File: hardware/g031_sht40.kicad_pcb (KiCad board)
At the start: 2 copper layers, 75 x 47 mm, 29 parts, among them J1 Screw_Terminal_01x02, J2 Conn_01x06_Pin, J3 Conn_01x02_Pin, J4 Screw_Terminal_01x02, J5 Conn_01x03_Pin, J6 Conn_01x04_Pin, J7 Conn_01x04_Pin, J8 Conn_01x08_Pin, SW1 SW_Push, U1 AEM10941 module, U2 SHT40 module, U3 STM32G031F6Px, U4 E-Ink display module

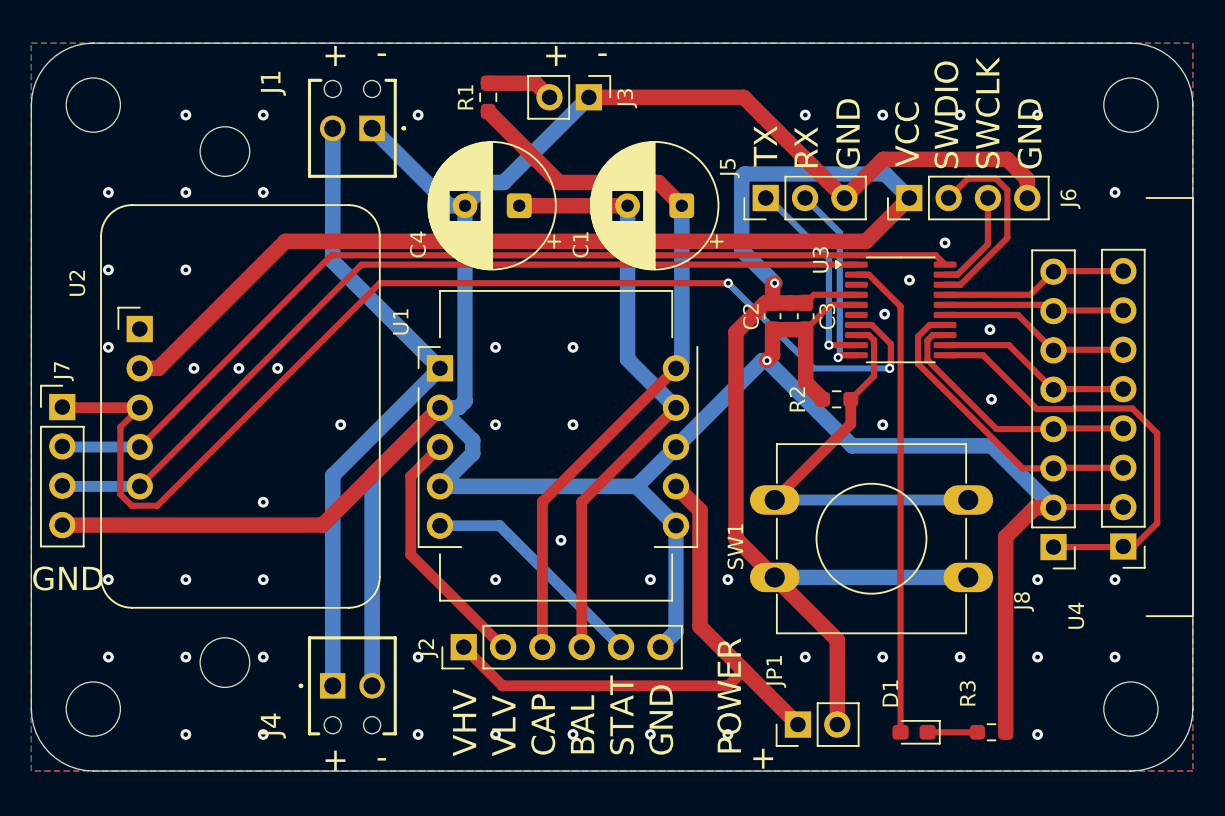
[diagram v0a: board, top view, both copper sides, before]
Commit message: Add Status pin connection
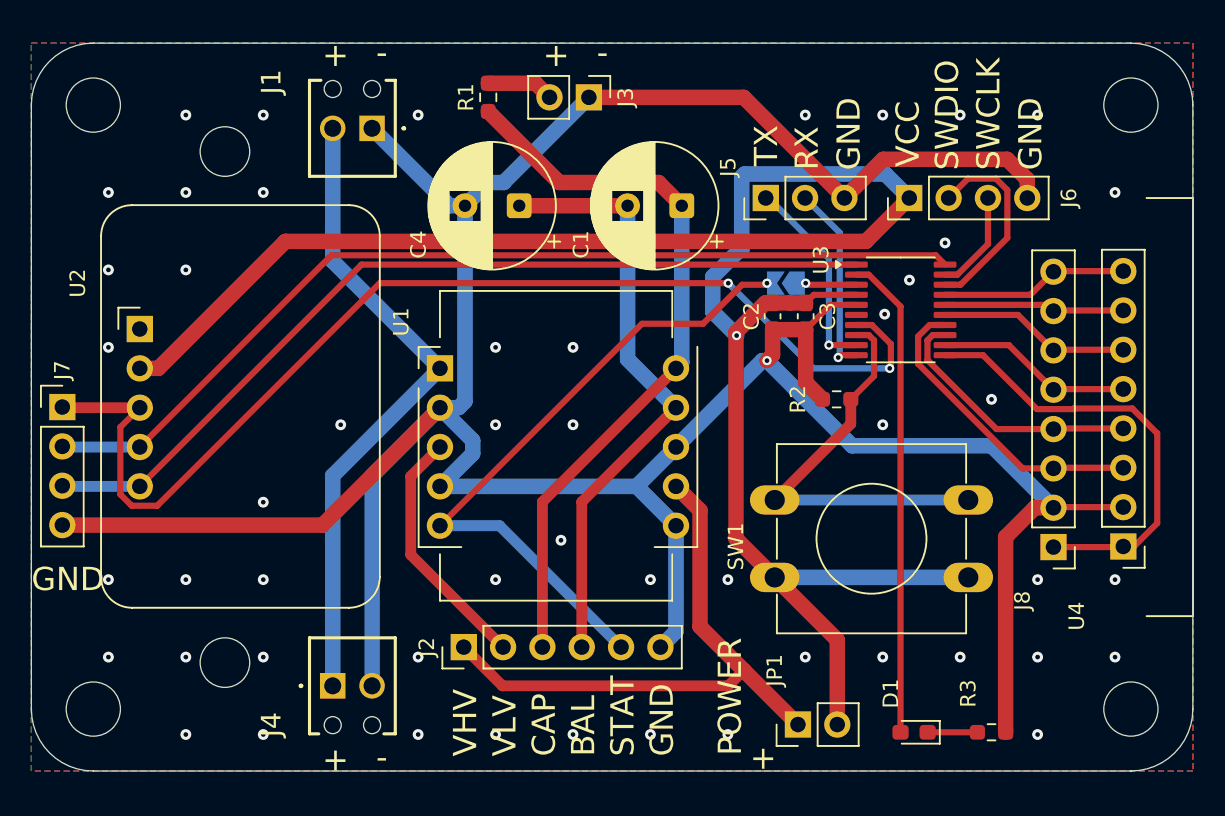
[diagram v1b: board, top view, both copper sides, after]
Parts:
- added JP2: Jumper_2_Open, Jumper:SolderJumper-2_P1.3mm_Open_TrianglePad1.0x1.5mm, B.Cu at (148.7, 68.5)
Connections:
- U3 pad 3: unconnected-(U3-PC15-Pad3) -> Net-(JP2-A)
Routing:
- net Net-(J2-Pin_5): track 14.9 -> 42.5 mm, vias 0 -> 1
- net Net-(JP2-A): track 0.00 -> 3.32 mm, vias 0 -> 1
- net +3V3: track 124.2 -> 126.9 mm
- net GND: vias 56 -> 52
